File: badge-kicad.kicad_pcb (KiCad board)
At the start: 4 copper layers, 153.5 x 153.5 mm, 100 parts, among them J2 JTAG, P1 TM1000, P2 CONN_02X20, P3 FTDI BACKUP, P4 USB_OTG, Q1 MNBT3904, SW1 SW_PUSH, U1 WS2812B, U10 WS2812B, U11 WS2812B, U12 WS2812B, U13 MKW01Z128, U14 FT232RL SSOP, U15 TPS76333, U16 MCP73831T-2ACI/OT, U2 WS2812B, U3 WS2812B, U4 WS2812B, U5 WS2812B, U6 WS2812B, U7 WS2812B, U8 WS2812B, U9 WS2812B, Y1 AWSCR-XTAL

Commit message: checkpoint v2 board
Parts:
- removed +VBAT: VBAT, Measurement_Points:Measurement_Point_Square-TH_Small
- removed GND: GND, Measurement_Points:Measurement_Point_Square-TH_Small
- removed R4: 120, Resistors_SMD:R_0805
- removed REF** (x2): MountingHole_3.2mm_M3, Mounting_Holes:MountingHole_3.2mm_M3
- removed REF** (x2): MountingHole_3.2mm_M3_DIN965, Mounting_Holes:MountingHole_3.2mm_M3_DIN965
- removed W4: LED_DATA_OUT, Measurement_Points:Measurement_Point_Round-TH_Small
- added ?: , logos:roman-head, F.Cu at (107.7, 93.0)
- added C16: 220pF, Capacitors_SMD:C_0805_HandSoldering, F.Cu at (87.8, 88.0)
- added C18: 0.01uF, Capacitors_SMD:C_0805_HandSoldering, F.Cu at (87.7, 81.4)
- added C19: 2pF, Capacitors_SMD:C_0805_HandSoldering, F.Cu at (102.2, 84.0)
- added H1: CONN_01X01, Mounting_Holes:MountingHole_3.2mm_M3_DIN965, F.Cu at (63.7, 73.0)
- added H2: CONN_01X01, Mounting_Holes:MountingHole_3.2mm_M3_DIN965, F.Cu at (130.2, 73.0)
- added H3: CONN_01X01, Mounting_Holes:MountingHole_3.2mm_M3_DIN965, F.Cu at (63.7, 129.0)
- added H4: CONN_01X01, Mounting_Holes:MountingHole_3.2mm_M3_DIN965, F.Cu at (130.2, 129.0)
- added H5: CONN_01X01, Mounting_Holes:MountingHole_3.2mm_M3_DIN965, F.Cu at (87.0, 30.0)
- added H6: CONN_01X01, Mounting_Holes:MountingHole_3.2mm_M3_DIN965, F.Cu at (103.5, 30.0)
- added L5: 15nH, Inductors_NEOSID:Neosid_Inductor_SM0603CG, F.Cu at (100.0, 47.8)
- added P5: LED OUT, Pin_Headers:Pin_Header_Straight_1x03, F.Cu at (75.8, 167.4)
- added SW2: SW_SPDT, Buttons_Switches_SMD:SW_SPDT_PCM12, F.Cu at (147.5, 149.7)
- added TP4: VBAT, Measurement_Points:Measurement_Point_Square-TH_Small, B.Cu at (133.1, 164.6)
- added TP5: GND, Measurement_Points:Measurement_Point_Square-TH_Small, B.Cu at (126.7, 164.5)
- C1, C10, C11, C12, C2, C20, C21, C3, C4, C5, C6, C7, C8, C9: value 100nF -> 0.1uF
- C14, C15: footprint Capacitors_SMD:C_0805_HandSoldering -> Capacitors_SMD:C_1206
- C24: value 100pF -> 7.5pF
- C25: value 7.5pF -> 5.6pF
- C26: value 5.6pF -> 100pF
- C28: value 1.2pF -> 3.3pF
- C29: value 2.0pF -> 1uF
- D2: value BLUE SDIO -> GREEN SDIO
- L1: value 0.0047 uH -> 4.7nH; footprint Inductors_NEOSID:Neosid_Inductor_SM1206 -> Inductors_NEOSID:Neosid_Inductor_SM0603CG
- L2: value 0.0068 uH -> 33nH; footprint Inductors_NEOSID:Neosid_Inductor_SM1206 -> Inductors_NEOSID:Neosid_Inductor_SM0603CG
- L3: footprint Inductors_NEOSID:Neosid_Inductor_SM1206 -> Inductors_NEOSID:Neosid_Inductor_SM0603CG
- L4: value 15 NH -> 0.0068 uH; footprint Inductors_NEOSID:Neosid_Inductor_SM1206 -> Inductors_NEOSID:Neosid_Inductor_SM0603CG
- P4: value USB_OTG -> USB_MICRO_RIGHT; footprint Connectors:USB_Micro-B -> MF_Connectors:MF_Connectors-MICROUSB-RIGHT; moved to B.Cu
- Q1: value MNBT3904 -> NPN_BJT_SOT-23-3; footprint TO_SOT_Packages_SMD:SOT-23 -> MF_Discrete_Semiconductor:MF_Discrete_Semiconductor-SOT-23-3
- SW1: value SW_PUSH -> RESET; footprint Buttons_Switches_SMD:SW_SPST_B3S-1000 -> MF_Switches:MF_Switches-TACT4.2MM
- TP1: footprint Measurement_Points:Measurement_Point_Square-TH_Small -> Measurement_Points:Measurement_Point_Round-TH_Small
- U1, U10, U11, U12, U2, U3, U4, U5, U6, U7, U8, U9: footprint LEDs:LED_WS2812B-PLCC4 -> MF_LEDs:MF_LEDs-WS2812B
- U15: value TPS76333 -> MF-REG-SOT235-3.3V-300mA; moved to B.Cu
- U16: moved to B.Cu
- moved P1 107.5 mm to (38.3, 106.9)
- moved W1 94.7 mm to (72.5, 135.0)
- moved W2 93.7 mm to (72.5, 141.0)
- moved W3 93.3 mm to (72.5, 147.0)
- moved J2 78.0 mm to (88.5, 52.2), turned to 0 degrees
- moved C29 65.0 mm to (116.0, 151.8)
- moved U14 42.5 mm to (121.8, 103.5)
- moved C32 40.0 mm to (128.5, 93.8), turned to 90 degrees
- moved R8 38.3 mm to (156.2, 119.5), turned to 180 degrees
- moved R13 37.1 mm to (135.6, 91.0), turned to 0 degrees
- moved D3 34.3 mm to (140.5, 91.0)
- moved R15 33.0 mm to (82.5, 157.6), turned to 0 degrees
- moved Y1 31.8 mm to (104.0, 96.0), turned to 270 degrees
- moved R14 28.9 mm to (135.6, 84.9), turned to 180 degrees
- moved W14 28.9 mm to (94.5, 141.0)
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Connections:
- C23 pad 2: Net-(C23-Pad2) -> Net-(C19-Pad1)
- C24 pad 2: Net-(C24-Pad2) -> GND
- C26 pad 1: Net-(C24-Pad1) -> Net-(C26-Pad1)
- C26 pad 2: GND -> Net-(C25-Pad1)
- C27 pad 1: Net-(C24-Pad2) -> Net-(C26-Pad1)
- C29 pad 1: Net-(C23-Pad1) -> VCC
- L1 pad 2: Net-(C23-Pad1) -> Net-(C19-Pad1)
- L2 pad 1: Net-(C23-Pad2) -> VR_PA
- L2 pad 2: Net-(C25-Pad1) -> Net-(C19-Pad1)
- L3 pad 1: Net-(C25-Pad1) -> Net-(C23-Pad1)
- L4 pad 1: Net-(C24-Pad2) -> Net-(C24-Pad1)
- L4 pad 2: Net-(A1-Pad2) -> Net-(C25-Pad1)
- R1 pad 2: Net-(Q1-Pad2) -> Net-(Q1-PadP$3)
- SP1 pad 2: Net-(Q1-Pad2) -> Net-(Q1-PadP$3)
- U13 pad 42: Net-(U13-Pad42) -> VR_PA
- U15 pad 5: VCC -> Net-(SW2-Pad1)
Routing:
- net Net-(P5-Pad2): track 0.00 -> 192.2 mm, vias 0 -> 1
- net PTB0: track 204.1 -> 102.7 mm, vias 2 -> 3
- net RESET_TGTMCU: track 147.2 -> 54.4 mm, vias 1 -> 2
- net VBAT: track 611.6 -> 530.8 mm
- net VUSB: track 249.5 -> 168.9 mm, vias 5 -> 4
- net Net-(U6-Pad2): track 66.0 -> 0.00 mm
- net VCC: track 480.7 -> 417.3 mm, vias 7 -> 6
- net Net-(Q1-Pad1): track 57.9 -> 0.00 mm
- net +3V3: track 70.1 -> 13.4 mm, vias 2 -> 0
- net Net-(U10-Pad4): track 55.7 -> 0.00 mm, vias 2 -> 0
- net Net-(P3-Pad6): track 27.2 -> 82.5 mm, vias 0 -> 1
- net Net-(U11-PadP$2): track 0.00 -> 54.9 mm
- net Net-(U6-PadP$2): track 0.00 -> 54.5 mm
- net Net-(U10-Pad2): track 52.4 -> 0.00 mm, vias 2 -> 0
- net Net-(U10-PadP$2): track 0.00 -> 51.0 mm
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- added copper zone on F.Cu, net GND
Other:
- copper layers 4 -> 2
- board text added: "+"
- board text added: "+V"
- board text added: "+VBAT"
- board text added: "-"
- board text added: "CTS"
- board text added: "DATA"
- board text added: "DISPLAY"
- board text added: "GND"
- board text added: "HAX"
- board text added: "John Adams @netik (PCB, HW, SW) Bill Paul (HW, Drivers, Board bringup, SW) Egan Hirvela (Game Mechanics) Matthew Harris (Art, Character Design) https://retina.net/dc25badge"
- board text added: "MISO"
- board text added: "MOSI"
- board text added: "PTA4"
- board text added: "PTB1"
- board text added: "PTC1"
- board text added: "PTC3"
- board text added: "PTC4"
- board text added: "PTD6"
- board text added: "RTS"
- board text added: "RX"
- board text added: "SCLK"
- board text added: "SPQR Badge Prototype - Rev 2 Defcon 25 (2017) HAIL CAESAR!"
- board text added: "TX"
- board text added: "VCC"
- board text added: "WS2812B STRIP OUT"
- board text removed: "RESET"
- board text removed: "SQPR Badge Prototype - Rev 1 Defcon 25 (2017) John Adams @netik (PCB, HW, SW) Bill Paul (HW, Drivers, Board bringup, SW) Egan Hirvela (Game Mechanics) Matthew Harris (Art, Character Design) Based on ChibiOS RTC HAIL CAESAR! Made in San Francisco"

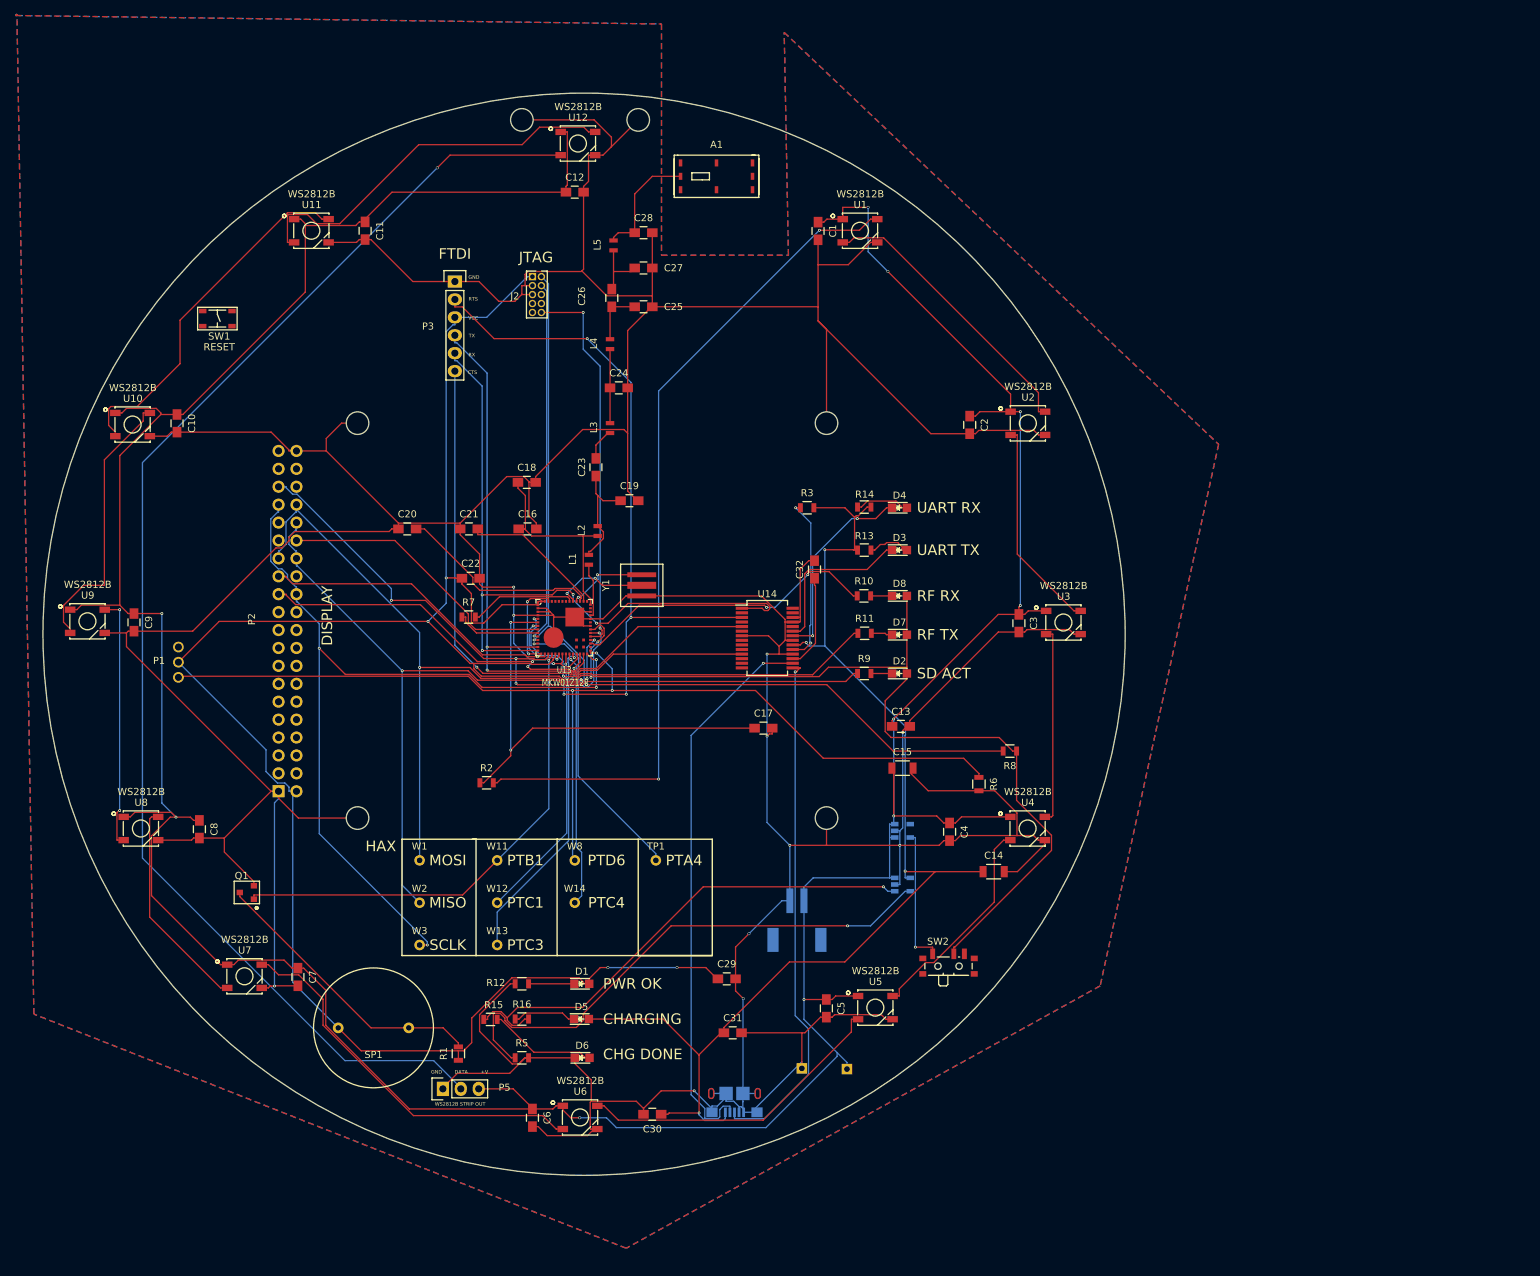
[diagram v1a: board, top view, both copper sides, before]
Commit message: new board shape, now with DAC, audio amp, and joypad
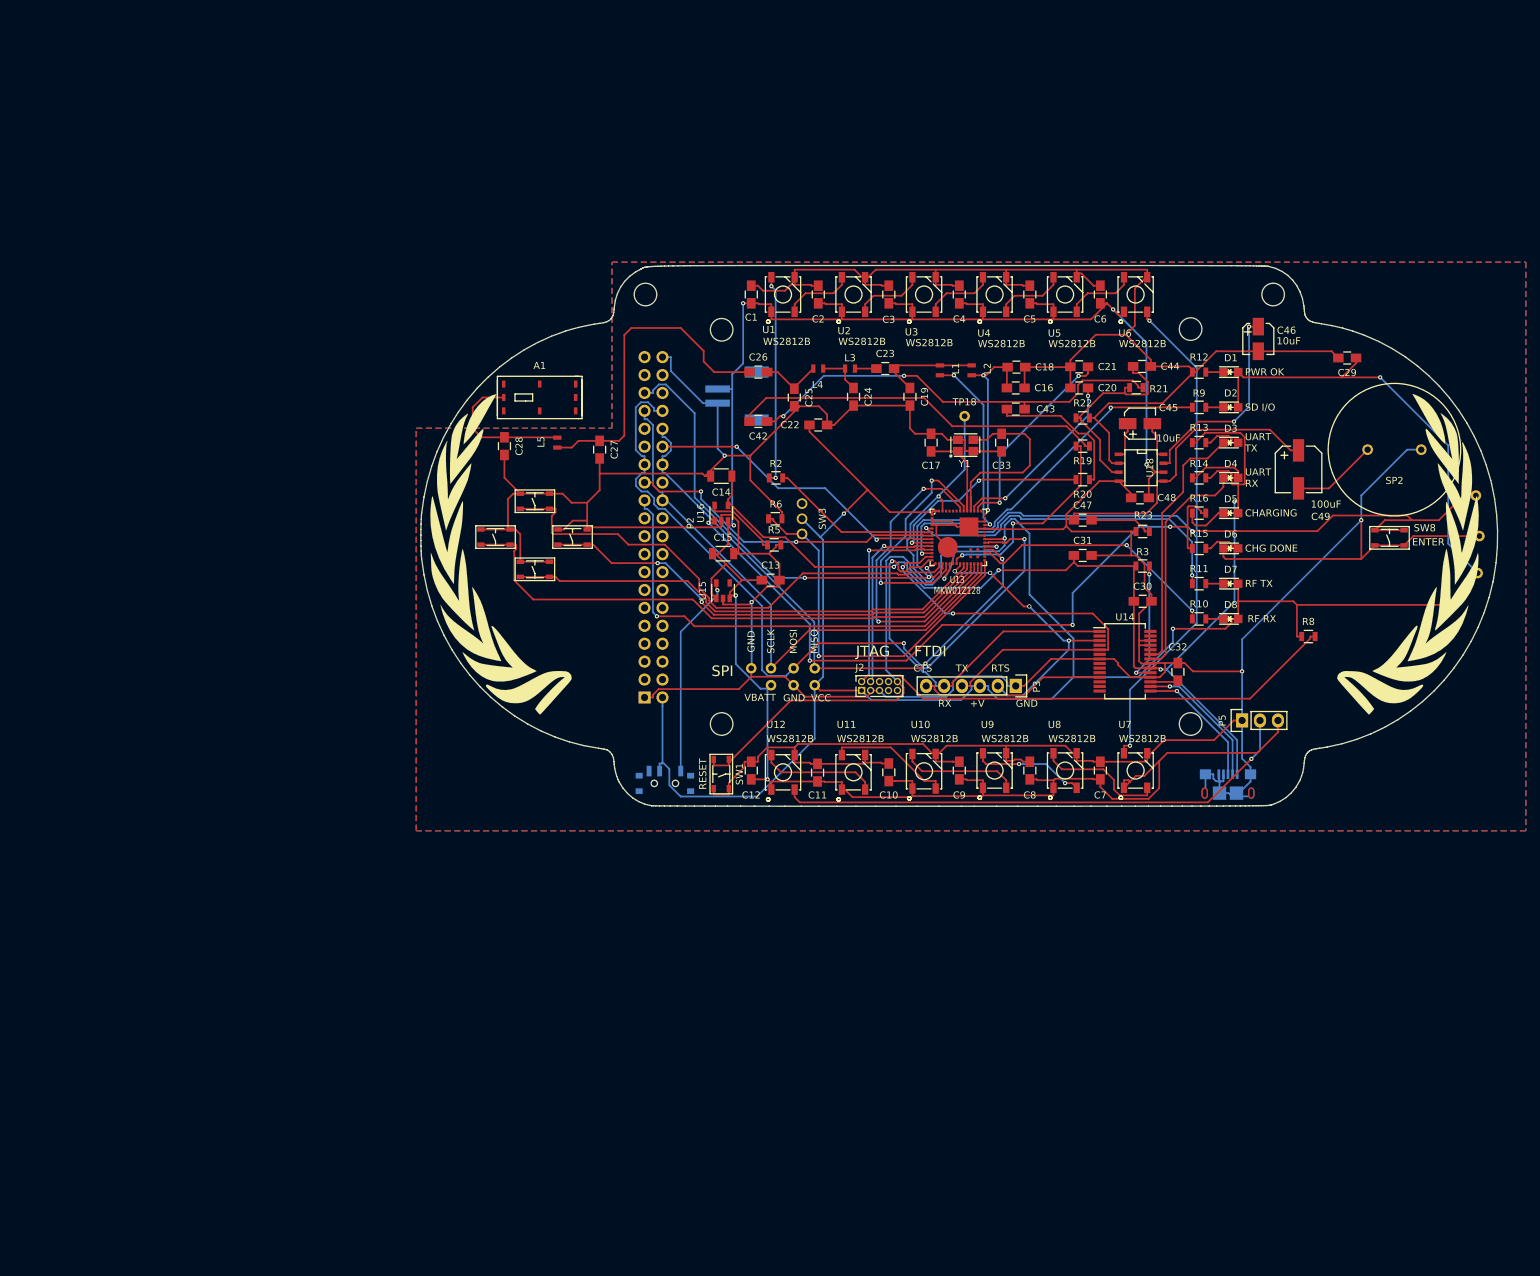
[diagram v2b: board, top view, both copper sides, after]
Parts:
- removed the ? at (107.7, 93.0)
- removed P1: TM1000, jna-parts:TM1000
- removed Q1: NPN_BJT_SOT-23-3, MF_Discrete_Semiconductor:MF_Discrete_Semiconductor-SOT-23-3
- removed R1: 1K, Resistors_SMD:R_0805
- removed R7: 100, Resistors_SMD:R_0805
- removed SP1: TDK PS1720P02, jna-parts:TDK_PS1720PD2
- removed W1: SPI_CH1_MOSI, Measurement_Points:Measurement_Point_Round-TH_Small
- removed W11: PTB1, Measurement_Points:Measurement_Point_Round-TH_Small
- removed W12: PTC1, Measurement_Points:Measurement_Point_Round-TH_Small
- removed W13: PTC3, Measurement_Points:Measurement_Point_Round-TH_Small
- removed W14: PTC4, Measurement_Points:Measurement_Point_Round-TH_Small
- removed W2: SPI_CH1_MISO, Measurement_Points:Measurement_Point_Round-TH_Small
- removed W3: SPI_CH1_SCLK, Measurement_Points:Measurement_Point_Round-TH_Small
- removed W8: PTD6, Measurement_Points:Measurement_Point_Round-TH_Small
- added ?: , logos:roman-head-small, B.Cu at (102.8, 86.6)
- added ?: , logos:laurel_right, F.Cu at (214.6, 91.5)
- added ?: , logos:laurel, F.Cu at (82.0, 91.5)
- added C33: 11pF, Capacitors_SMD:C_0805_HandSoldering, F.Cu at (155.0, 75.8)
- added C42: 10uF, Capacitors_SMD:C_0805_HandSoldering, F.Cu at (120.5, 72.8)
- added C43: 10uF, Capacitors_SMD:C_0805_HandSoldering, F.Cu at (157.0, 71.0)
- added C44: 0.01uF, Capacitors_SMD:C_0805_HandSoldering, F.Cu at (174.9, 65.0)
- added C45: 10uF, MF_Passives:MF_Passives-CP4MM, F.Cu at (174.7, 73.1)
- added C46: 10uF, MF_Passives:MF_Passives-CP4MM, F.Cu at (191.4, 61.1)
- added C47: .047uF, Capacitors_SMD:C_0805_HandSoldering, F.Cu at (166.5, 86.8)
- added C48: 10uF, Capacitors_SMD:C_0805_HandSoldering, F.Cu at (174.7, 83.6)
- added C49: 100uF, MF_Passives:MF_Passives-CP6.3MM, F.Cu at (197.1, 79.6)
- added R19: 1k, Resistors_SMD:R_0805, F.Cu at (166.5, 76.3)
- added R20: 1k, Resistors_SMD:R_0805, F.Cu at (166.5, 81.0)
- added R21: 100k, Resistors_SMD:R_0805, F.Cu at (174.1, 68.0)
- added R22: 1k, Resistors_SMD:R_0805, F.Cu at (166.5, 72.3)
- added R23: 10k, Resistors_SMD:R_0805, F.Cu at (175.0, 88.4)
- added SP2: MODEL TBD, jna-parts:SPEAKER_AST_01708MR_R, F.Cu at (210.7, 76.8)
- added SW3: TM1000, jna-parts:TM1000, F.Cu at (126.7, 86.6)
- added SW4: UP, MF_Switches:MF_Switches-TACT4.2MM, F.Cu at (88.9, 84.1)
- added SW5: DN, MF_Switches:MF_Switches-TACT4.2MM, F.Cu at (88.9, 93.7)
- added SW6: LEFT, MF_Switches:MF_Switches-TACT4.2MM, F.Cu at (83.3, 89.2)
- added SW7: RIGHT, MF_Switches:MF_Switches-TACT4.2MM, F.Cu at (94.2, 89.2)
- added SW8: ENTER, MF_Switches:MF_Switches-TACT4.2MM, F.Cu at (210.0, 89.3)
- added TP10: GND, Measurement_Points:Measurement_Point_Round-TH_Small, F.Cu at (125.5, 110.2)
- added TP17: SPI_CH1_SCLK, Measurement_Points:Measurement_Point_Round-TH_Small, F.Cu at (122.3, 107.8)
- added TP18: CLOCKOUT, Measurement_Points:Measurement_Point_Round-TH_Small, F.Cu at (149.8, 72.0)
- added TP19: SPI_CH1_MOSI, Measurement_Points:Measurement_Point_Round-TH_Small, F.Cu at (125.5, 107.8)
- added TP2: GND, Measurement_Points:Measurement_Point_Round-TH_Small, F.Cu at (222.8, 89.0)
- added TP20: SPI_CH1_MISO, Measurement_Points:Measurement_Point_Round-TH_Small, F.Cu at (128.5, 107.8)
- added TP3: VCC, Measurement_Points:Measurement_Point_Round-TH_Small, F.Cu at (128.5, 110.2)
- added TP9: VCC, Measurement_Points:Measurement_Point_Round-TH_Small, F.Cu at (222.5, 94.3)
- added U18: LM386, SMD_Packages:SOIC-8-N, F.Cu at (174.8, 79.3)
- C17: value 100uF -> 11pF
- P5: value LED OUT -> LED OUT (DNP)
- SW2: value SW_SPDT -> POWERON; moved to B.Cu
- TP4, TP5: footprint Measurement_Points:Measurement_Point_Square-TH_Small -> Measurement_Points:Measurement_Point_Round-TH_Small; moved to F.Cu
- U15, U16: moved to F.Cu
- Y1: value AWSCR-XTAL -> EXS00A-CS02368; footprint Crystals:AWSCR_XTAL -> jna-parts:Crystal_EXS00A-CS02368
- moved C6 141.8 mm to (169.0, 54.8), turned to 90 degrees
- moved U6 140.8 mm to (174.0, 54.8), turned to 90 degrees
- moved U8 131.3 mm to (164.0, 122.3), turned to 90 degrees
- moved U9 130.4 mm to (154.0, 122.3), turned to 90 degrees
- moved U7 129.7 mm to (174.0, 122.3), turned to 90 degrees
- moved R12 129.4 mm to (183.0, 65.8)
- moved TP1 127.3 mm to (222.3, 83.3)
- moved D1 126.5 mm to (187.5, 65.8)
- moved P5 124.8 mm to (189.1, 115.2)
- moved C29 124.5 mm to (204.0, 63.8), turned to 180 degrees
- moved U10 122.5 mm to (144.0, 122.4), turned to 90 degrees
- moved R15 120.7 mm to (183.0, 90.8)
- moved R16 119.9 mm to (183.0, 85.8)
- moved C9 118.9 mm to (149.0, 122.3), turned to 90 degrees
- moved C8 118.0 mm to (159.0, 122.3), turned to 90 degrees
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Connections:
- net Net-(TP1-Pad1) renamed SWENTER
- C17 pad 1: LEDS_IN -> Net-(C17-Pad1)
- H1 pad 1: GND -> Net-(H1-Pad1)
- H2 pad 1: GND -> Net-(H2-Pad1)
- H3 pad 1: GND -> Net-(H3-Pad1)
- H4 pad 1: GND -> Net-(H4-Pad1)
- H5 pad 1: GND -> Net-(H5-Pad1)
- H6 pad 1: GND -> Net-(H6-Pad1)
- SW1 pad P$1: (no net) -> GND
- SW1 pad P$2: (no net) -> RESET_TGTMCU
- SW1 pad P$3: (no net) -> GND
- SW1 pad P$4: (no net) -> RESET_TGTMCU
- U13 pad 16: DISP_DC -> SWUP
- U13 pad 18: PWM_SOUND -> RF_RESET
- U13 pad 23: Net-(U13-Pad23) -> SWDN
- U13 pad 24: Net-(U13-Pad24) -> SWR
- U13 pad 25: PWM_SOUND -> SWL
- U13 pad 26: Net-(U13-Pad26) -> DIO0
- U13 pad 46: Net-(U13-Pad46) -> Net-(C33-Pad1)
- U13 pad 47: Net-(U13-Pad47) -> Net-(C17-Pad1)
- U13 pad 48: Net-(R7-Pad2) -> RF_RESET
- U13 pad 49: Net-(U13-Pad49) -> DIO0
- U13 pad 9: RF_RESET -> DACOUT
- Y1 pad 1: Net-(U13-Pad46) -> Net-(C17-Pad1)
- Y1 pad 2: Net-(U13-Pad47) -> GND
- Y1 pad 3: GND -> Net-(C33-Pad1)
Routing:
- net VBAT: track 530.8 -> 313.8 mm, vias 10 -> 6
- net Net-(P5-Pad2): track 192.2 -> 74.7 mm
- net GND: track 932.7 -> 823.6 mm, vias 12 -> 4
- net TILTSENS: track 151.5 -> 54.6 mm, vias 3 -> 1
- net Net-(R2-Pad2): track 119.8 -> 29.6 mm
- net VCC: track 417.3 -> 331.2 mm, vias 6 -> 5
- net SWL: track 0.00 -> 80.9 mm
- net SWUP: track 0.00 -> 72.0 mm
- net SWDN: track 0.00 -> 68.3 mm
- net Net-(R5-Pad1): track 76.6 -> 10.6 mm, vias 1 -> 0
- net SWR: track 0.00 -> 65.9 mm, vias 0 -> 2
- net UART0_CTS: track 105.4 -> 40.6 mm, vias 5 -> 4
- net Net-(C42-Pad1): track 0.00 -> 61.0 mm, vias 0 -> 2
- net Net-(P4-Pad2): track 79.5 -> 19.7 mm
- net SWENTER: track 41.0 -> 99.8 mm, vias 1 -> 2
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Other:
- board size 153.5 x 153.5 mm -> 152.7 x 76.7 mm
- net class Default: clearance 0.13 -> 0.2; trace_width 0.13 -> 0.25; via_dia 0.4 -> 0.6; via_drill 0.305 -> 0.4
- rule trace_clearance: 0.13 -> 0.2
- rule trace_min: 0.13 -> 0.25
- rule via_min_drill: 0.305 -> 0.3
- board text added: "LEDs"
- board text added: "SD I/O"
- board text added: "SPI"
- board text added: "VBATT"
- board text removed: "+"
- board text removed: "+VBAT"
- board text removed: "-"
- board text removed: "DISPLAY"
- board text removed: "HAX"
- board text removed: "John Adams @netik (PCB, HW, SW) Bill Paul (HW, Drivers, Board bringup, SW) Egan Hirvela (Game Mechanics) Matthew Harris (Art, Character Design) https://retina.net/dc25badge"
- board text removed: "PTA4"
- board text removed: "PTB1"
- board text removed: "PTC1"
- board text removed: "PTC3"
- board text removed: "PTC4"
- board text removed: "PTD6"
- board text removed: "SD ACT"
- board text removed: "SPQR Badge Prototype - Rev 2 Defcon 25 (2017) HAIL CAESAR!"
- board text removed: "WS2812B STRIP OUT"
